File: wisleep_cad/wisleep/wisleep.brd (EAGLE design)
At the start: 53.2 x 54.4 mm, 23 parts, among them IC1 STM32F10XCXT6, U1 MAX1555, X1 8MHz

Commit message: some more cad
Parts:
- removed U1: MAX1555, SparkFun-PowerIC:SOT23-5
- added U$3: BQ24072VSON16, robot:VSON16
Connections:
- new net BAT1: U$3.2
- new net BAT2: U$3.3
- new net IN: U$3.13
- new net OUT1: U$3.10
- new net OUT2: U$3.11
- new net PAD_GND: U$3.PAD
- net GND: now also U$3.8
- net GND2: no longer U1.2
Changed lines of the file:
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@@
 <element name="C2" library="robot" package="C0402" value="34pF" x="16.51" y="13.97" rot="R90"/>
 <element name="U$1" library="SparkFun-Connectors" package="2X4" value="M04X2" x="44.821971875" y="11.058025" rot="R45"/>
-<element name="U1" library="SparkFun-PowerIC" package="SOT23-5" value="MAX1555" x="17.78" y="41.91" rot="R180"/>
 <element name="U$2" library="robot" package="10-TDFN-EP" value="MAX8815AOWNMAX8815A" x="35.56" y="48.26" rot="R180"/>
 <element name="MDL1" library="ESP8266-ESP12E" package="ESP8266-ESP12E" value="" x="29.46" y="35.81" rot="R270"/>
@@
 </element>
 <element name="JP1" library="SparkFun-Connectors" package="1X02_LOCK" value="M02LOCK" x="17.78" y="46.99" rot="R90"/>
+<element name="U$3" library="robot" package="VSON16" value="BQ24072VSON16" x="35.56" y="43.18"/>
 </elements>
 <signals>
@@
 <contactref element="U$2" pad="THERM"/>
 <contactref element="J1" pad="1"/>
+<contactref element="U$3" pad="8"/>
 <wire x1="35.56" y1="48.26" x2="37.04" y2="49.285" width="0" layer="19" extent="1-1"/>
-<wire x1="26.67" y1="49.99" x2="37.04" y2="49.285" width="0" layer="19" extent="1-1"/>
-<wire x1="26.05" y1="27.94" x2="35.56" y2="48.26" width="0" layer="19" extent="1-1"/>
+<wire x1="26.67" y1="49.99" x2="35.56" y2="48.26" width="0" layer="19" extent="1-1"/>
+<wire x1="26.05" y1="27.94" x2="26.67" y2="49.99" width="0" layer="19" extent="1-1"/>
 <wire x1="24.82" y1="25.11" x2="26.05" y2="27.94" width="0" layer="19" extent="1-1"/>
 <wire x1="18.07" y1="27.36" x2="24.82" y2="25.11" width="0" layer="19" extent="1-1"/>
@@
 <wire x1="39.9252375" y1="4.37280625" x2="35.284425" y2="2.306584375" width="0" layer="19" extent="1-1"/>
 <wire x1="48.414071875" y1="12.854075" x2="39.9252375" y2="4.37280625" width="0" layer="19" extent="1-1"/>
+<wire x1="37.31" y1="42.43" x2="12.08" y2="13.97" width="0" layer="19" extent="1-1"/>
 </signal>
 <signal name="3.3V">
@@
 <contactref element="J1" pad="2"/>
 <contactref element="JP1" pad="2"/>
-<contactref element="U1" pad="2"/>
 <wire x1="17.78" y1="49.7078" x2="21.87" y2="46.99" width="0" layer="19" extent="1-1"/>
-<wire x1="17.78" y1="43.2101" x2="21.87" y2="46.99" width="0" layer="19" extent="1-1"/>
+</signal>
+<signal name="BAT1">
+<contactref element="U$3" pad="2"/>
+</signal>
+<signal name="BAT2">
+<contactref element="U$3" pad="3"/>
+</signal>
+<signal name="IN">
+<contactref element="U$3" pad="13"/>
+</signal>
+<signal name="OUT1">
+<contactref element="U$3" pad="10"/>
+</signal>
+<signal name="PAD_GND">
+<contactref element="U$3" pad="PAD"/>
+</signal>
+<signal name="OUT2">
+<contactref element="U$3" pad="11"/>
 </signal>
 </signals>

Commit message: more cadding
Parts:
- added U$4: MIC5239-3.3v, robot:SOT223
- added U$5: MIC5239-3.3v, robot:MSOP08
- moved U$2 25.0 mm to (11.4, 41.9)
- moved U$3 16.6 mm to (19.1, 41.9)
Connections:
- net POW renamed POWDC
- removed net GND2: J1.2, JP1.2
- new net OUT: U$4.3, U$5.4
- net GND: now also U$4.2, U$4.4, U$5.5, U$5.6, U$5.7, U$5.8
- net IN: now also U$4.1, U$5.3

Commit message: even moar cad
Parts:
- added C3: 0.1uF, robot:C0402
- added C5: 10uF, robot:C0402
- added C6: 22uF, robot:EIA3216
- added GY-85: (no value), robot:1X08
- added R1, R2, R6, R7: 100k, SparkFunEagle-6-6-07:C0402
- added R3, R4, R5, R8: 0, SparkFunEagle-6-6-07:C0402
- added U$6: (no value), robot:INDUCTOR-3014
- added X2: 32kHz, robot:CRYSTAL_SMD_2X0.6
- U$2: value MAX8815AOWNMAX8815A -> MAX8815A10TDFNEP
- moved C19 24.1 mm to (34.0, 10.5), turned to 24 degrees
- moved JP1 20.3 mm to (38.0, 48.5), turned to 156 degrees
- moved C12 18.9 mm to (16.0, 13.5), turned to 270 degrees
- moved LED2 14.8 mm to (17.0, 3.75), turned to 66 degrees
- moved R16 13.2 mm to (17.5, 5.00), turned to 156 degrees
- moved L1 12.2 mm to (20.5, 16.0), flipped to the bottom, turned to 180 degrees
- moved C13 10.8 mm to (20.5, 14.5), flipped to the bottom
- moved C18 8.55 mm to (18.0, 8.50), turned to 90 degrees
- moved U$3 8.31 mm to (27.0, 39.5), turned to 270 degrees
- moved C2 7.14 mm to (13.5, 7.50), turned to 180 degrees
- moved U$4 6.80 mm to (17.8, 33.0), turned to 0 degrees
- moved C1 6.10 mm to (13.5, 9.50), turned to 180 degrees
- moved X1 5.55 mm to (22.5, 8.50)
- moved C17 5.48 mm to (27.0, 8.50)
- moved C11 5.45 mm to (25.0, 22.5), turned to 90 degrees
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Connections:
- net SPI_MISO renamed N$18
- net SPI_MOSI renamed N$20
- removed net BAT1: U$3.2
- removed net BAT2: U$3.3
- removed net BATT: U$2.3
- removed net IN: U$3.13, U$4.1, U$5.3
- removed net OUT: U$4.3, U$5.4
- removed net OUT1: U$3.10
- removed net OUT2: U$3.11
- removed net PAD_GND: U$3.PAD
- removed net SPI_CS: IC1.14
- removed net SPI_SCK: IC1.15
- removed net SWDCLK: U$1.8
- new net 5V: R8.1
- new net BAT+: JP1.1, U$3.2, U$3.3
- new net BAT-: JP1.2
- new net G_INT(NC): GY-85.1
- new net M_DRDY(NC): GY-85.3
- new net N$10: U$3.15
- new net N$11: U$3.12
- new net N$12: U$3.16
- new net N$13: R4.2, U$4.3
- new net N$14: R5.2, U$5.4
- new net N$15: U$2.1, U$2.2, U$6.P$2
- new net N$16: R6.1, U$2.7
- new net N$17: IC1.11
- new net N$19: R7.2, U$2.8
- new net N$21: IC1.27
- new net N$22: IC1.33
- new net N$23: IC1.38
- new net N$26: IC1.41
- new net N$27: IC1.40
- new net N$28: IC1.29
- new net N$4: R3.1, U$3.10, U$3.11
- new net N$6: U$3.4
- new net N$8: U$3.6
- new net N$9: U$3.5
- new net NCHG: IC1.21, R1.2, U$3.9
- new net NPGOOD: IC1.22, R2.2, U$3.7
- new net V+: C5.1, R3.2, U$2.3, U$4.1, U$5.3, U$6.P$1
- new net VCC: MDL1.8, R5.1
- new net WIFI_BL15: IC1.26, MDL1.10
- new net WIFI_BL2: IC1.20, MDL1.11
- new net WIFI_BOOT: IC1.18, MDL1.12
- new net WIFI_ENA: IC1.25, MDL1.3
- new net WIFI_IO4: IC1.15, MDL1.13
- new net WIFI_IO5: IC1.14, MDL1.14
- new net WIFI_POW_ENA: IC1.32, U$5.1
- new net WIFI_RES: IC1.19, MDL1.1
- net 3.3V: now also GY-85.7, R1.1, R2.1, R4.1; no longer LED2.A
- net 5V_ENA: now also IC1.39, U$2.4; no longer IC1.29
- net ACC_INT1: now also GY-85.2
- net GND: now also C3.2, C5.2, C6.C, GY-85.6, LED2.C, MDL1.9, R7.1, U$3.PAD
- net N$1: now also X2.P$1
- net N$2: now also X2.P$2
- net N$3: now also C3.1, C6.A, R6.2, R8.2
- net N$5: now also LED2.A; no longer LED2.C
- net POWDC: now also U$3.13
- net SCL: now also GY-85.5, IC1.42; no longer IC1.21
- net SDA: now also GY-85.4, IC1.43; no longer IC1.22
- net SWCLK: now also U$1.8
- net WIFI_RX: now also MDL1.16
- net WIFI_TX: now also MDL1.15
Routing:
- net 3.3V: track 0.00 -> 81.7 mm, vias 0 -> 5
- net SWCLK: track 0.00 -> 45.7 mm, vias 0 -> 2
- net V+: track 0.00 -> 43.5 mm
- net SWDIO: track 0.00 -> 41.1 mm, vias 0 -> 1
- net WIFI_POW_ENA: track 0.00 -> 37.5 mm, vias 0 -> 2
- net WIFI_RES: track 0.00 -> 33.2 mm, vias 0 -> 2
- net ACC_INT1: track 0.00 -> 33.0 mm, vias 0 -> 2
- net 5V_ENA: track 0.00 -> 30.8 mm, vias 0 -> 4
- net WIFI_RX: track 0.00 -> 30.0 mm
- net RST: track 0.00 -> 26.4 mm
- net WIFI_TX: track 0.00 -> 26.2 mm
- net WIFI_ENA: track 0.00 -> 26.0 mm, vias 0 -> 2
- net USART_TX: track 0.00 -> 24.8 mm, vias 0 -> 2
- net USART_RX: track 0.00 -> 23.7 mm
- net WIFI_IO5: track 0.00 -> 18.3 mm, vias 0 -> 2
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- added copper zone on layer 1, net BAT+
- added copper zone on layer 1, net GND
- added copper zone on layer 16, net GND
- added copper zone on layer 1, net N$15
- added copper zone on layer 1, net N$3
- added copper zone on layer 1, net N$4
- added copper zone on layer 1, net V+
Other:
- board size 53.2 x 54.4 mm -> 52.4 x 54.3 mm

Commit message: cadding soon to an end
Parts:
- removed R3, R5, R8: 0, SparkFunEagle-6-6-07:C0402
- added C14, C15, C16, C8, C9: 10uF, robot:C0402
- added C4, C7: 22uF, robot:EIA3216
- added JP2, JP3, JP4: M01PTH_LONGPAD, SparkFun-Connectors:1X01_LONGPAD
- added NTC1: 10kR, SparkFunEagle-6-6-07:C0402
- added R10: 100k, SparkFunEagle-6-6-07:C0402
- added R12: 1192R, SparkFunEagle-6-6-07:C0402
- added R13: 1113R, SparkFunEagle-6-6-07:C0402
- added R14: 22.5kR, SparkFunEagle-6-6-07:C0402
- added RSENS_5V, RSENS_BAT, RSENS_MAIN, RSENS_WIFI: 0, SparkFunEagle-6-6-07:C0402
- moved R1 1.12 mm to (24.0, 30.8)
- moved R2 1.03 mm to (25.2, 30.8)
- moved U$3 1.00 mm to (26.0, 39.5)
- renumbered R4 to RSENS_CPU
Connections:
- removed net N$10: U$3.15
- net 5V: now also JP3.1, RSENS_5V.1; no longer R8.1
- net BAT+: now also C4.A
- net BAT-: now also RSENS_BAT.2
- net GND: now also C14.2, C15.2, C16.2, C4.C, C7.C, C8.2, C9.2, JP4.1, NTC1.2, R12.1, R13.1, R14.1, RSENS_BAT.1, U$3.15, U$3.4, U$3.6
- net LAMP_IO: now also JP2.1
- net N$11: now also R12.2
- net N$12: now also R13.2
- net N$13: now also C14.1
- net N$14: now also C16.1, RSENS_WIFI.2; no longer R5.2
- net N$3: now also RSENS_5V.2; no longer R8.2
- net N$4: now also RSENS_MAIN.1; no longer R3.1
- net N$6: now also R14.2, U$3.14; no longer U$3.4
- net N$8: now also NTC1.1, U$3.1; no longer U$3.6
- net N$9: now also R10.2
- net POWDC: now also C8.1
- net V+: now also C15.1, C7.A, C9.1, R10.1, RSENS_MAIN.2; no longer R3.2
- net VCC: now also RSENS_WIFI.1; no longer R5.1
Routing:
- net NCHG: track 0.00 -> 26.5 mm, vias 0 -> 4
- net NPGOOD: track 0.00 -> 25.4 mm, vias 0 -> 4
- net LAMP_IO: track 0.00 -> 20.0 mm, vias 0 -> 2
- net 3.3V: track 81.7 -> 90.1 mm
- net N$6: track 0.00 -> 5.62 mm
- net 5V: track 0.00 -> 4.37 mm
- net N$14: track 1.42 -> 5.02 mm
- net N$12: track 0.00 -> 2.87 mm
- net N$13: track 0.77 -> 3.32 mm
- net V+: track 43.5 -> 46.0 mm
- net GND: track 5.92 -> 8.27 mm, vias 26 -> 87
- net N$4: track 0.00 -> 2.06 mm
- net VCC: track 6.74 -> 4.82 mm
- net BAT-: track 0.00 -> 1.87 mm
- net N$8: track 0.00 -> 1.76 mm
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- added copper zone on layer 1, net POWDC

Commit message: wisleep cad rev A - 2 fab
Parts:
- moved U$7 48.3 mm to (38.6, 38.5)
- moved R2 0.25 mm to (25.5, 30.8)
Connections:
- removed net N$18: IC1.16
- removed net N$7: U$1.4
- new net DBG_IO: IC1.16, U$1.4
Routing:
- net DBG_IO: track 0.00 -> 20.4 mm, vias 0 -> 1
- net WIFI_IO5: track 18.3 -> 19.1 mm
- net USART_RX: track 23.7 -> 24.3 mm
- net GND: track 8.27 -> 8.75 mm, vias 87 -> 99
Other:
- board size 52.4 x 54.3 mm -> 52.1 x 54 mm
- board text added: "3.3V"
- board text added: "32kHz"
- board text added: "5V"
- board text added: "8MHz"
- board text added: "BAT+"
- board text added: "BAT-"
- board text added: "DC5V"
- board text added: "DEBUG"
- board text added: "GY-85"
- board text added: "ILIM"
- board text added: "ISET"
- board text added: "LED"
- board text added: "NTC"
- board text added: "RESET"
- board text added: "REV A"
- board text added: "S5V"
- board text added: "SBAT"
- board text added: "SCPU"
- board text added: "SMAIN"
- board text added: "STM32F1"
- board text added: "SWIFI"
- board text added: "TMR"
- board text added: "WS5V"
- board text added: "WSGND"
- board text added: "WSSIG"
- board text added: "wisleep"
- board text added: "www.pelleplutt.com"

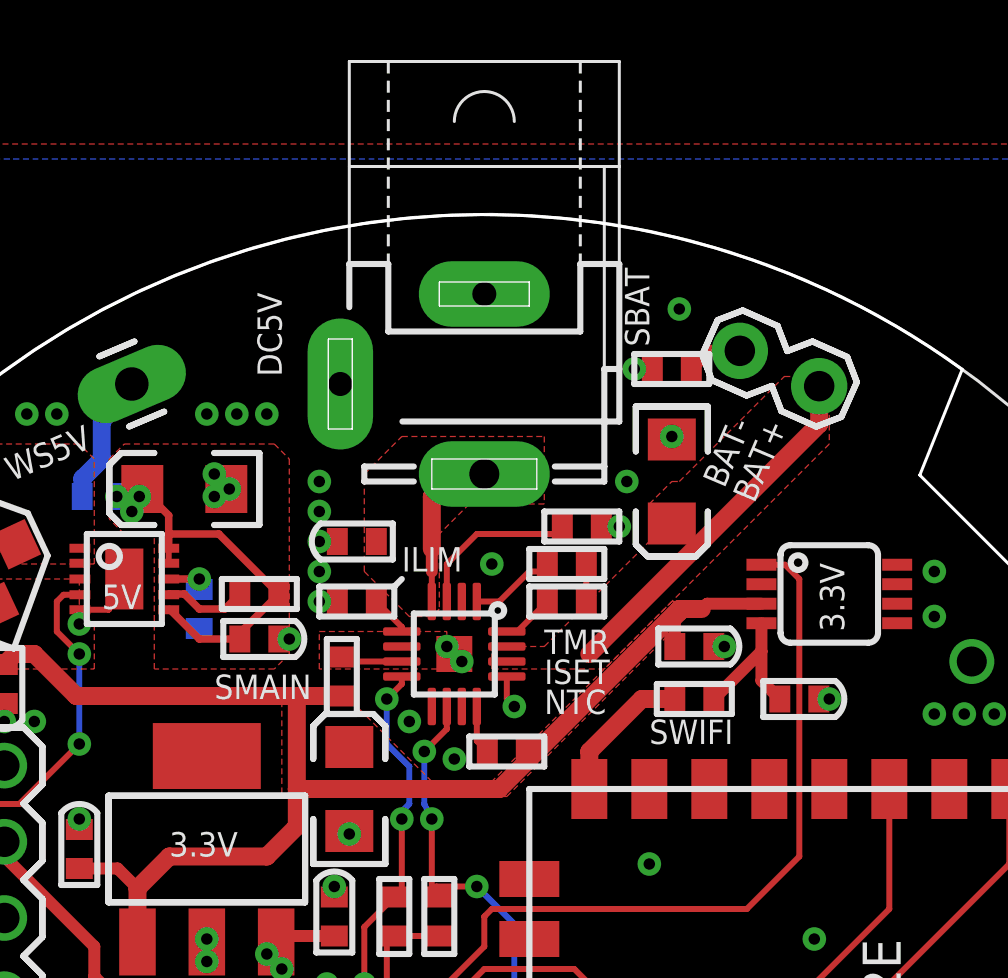
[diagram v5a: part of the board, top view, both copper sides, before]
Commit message: fixed up dc jack holes, resent to fab
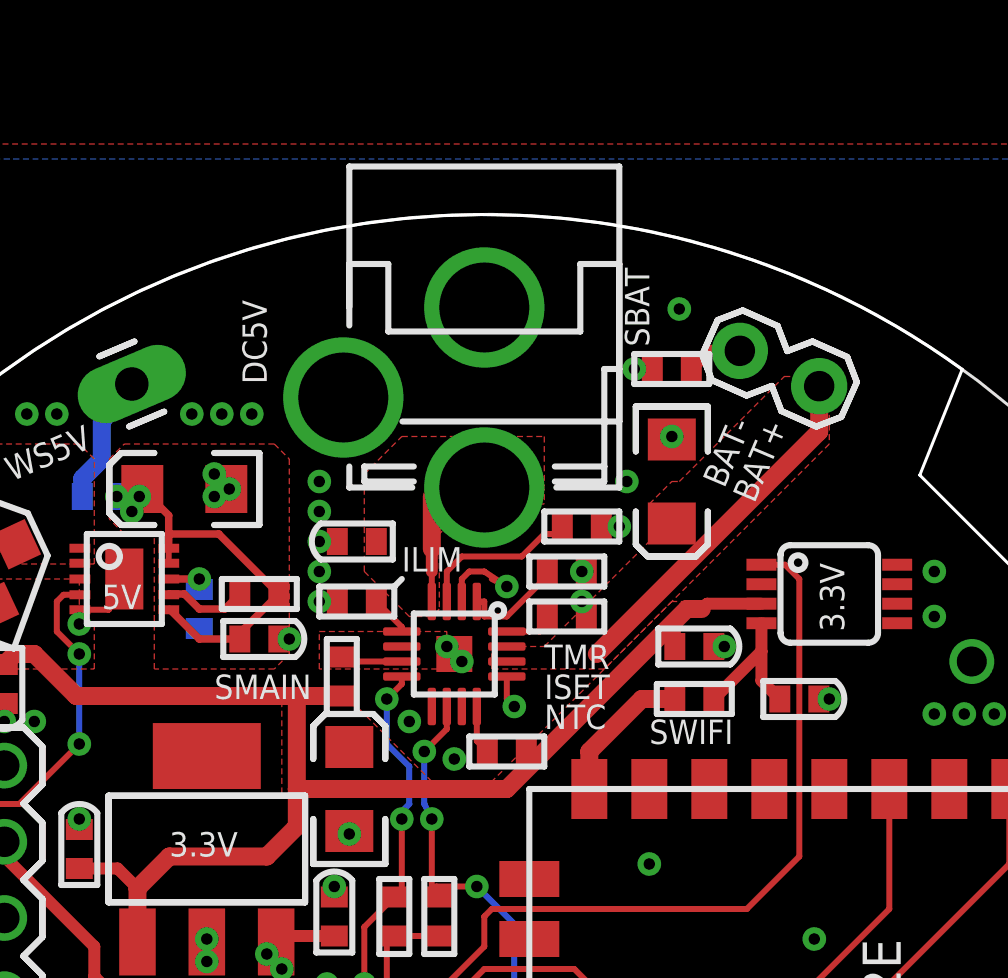
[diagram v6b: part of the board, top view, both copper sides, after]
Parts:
- removed J1: (no value), con-jack:SPC4077
- added U$8: (no value), SparkFunEagle-6-6-07:POWER_JACK_PTH
- moved NTC1 0.50 mm to (29.8, 40.8)
- moved R13 0.25 mm to (29.8, 42.2)
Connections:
- net GND: now also U$8.GND; no longer J1.1
- net POWDC: now also U$8.PWR; no longer J1.3
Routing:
- net GND: track 8.75 -> 11.1 mm, vias 99 -> 101
- net POWDC: track 5.40 -> 3.50 mm
- net N$12: track 2.87 -> 3.54 mm
